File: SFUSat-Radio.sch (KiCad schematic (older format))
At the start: 1 part

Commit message: added jumpers for regulater EN and a jumper for fixing PA_ADJ. Connceted TRX_SIG to GPIO0
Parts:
- added JP? (x4): JUMPER, symbol JUMPER
- added R?: 457.8, symbol R
- added R?: 1k, symbol R
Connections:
- net labels added: EN_1V8, EN_3V3, EN_3V6, VCC_3.3, VCC_6.0_PW_IN
- wire segments 26 -> 38
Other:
- note added: "Jumper to fix ADJ to 2.25V or drive it externally.\nVoltage devider is 0.467=R_top * (G_bottom + 1/50k). \nSee SKY datasheet for 50k figure."
- note added: "Jumpers to fix regulators on or enable them externally"
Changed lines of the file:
@@
 F6 "SCLK" I L 3700 4600 60
 F7 "MISO" I L 3700 5100 60
-F8 "GPIO0" I L 3700 4300 60
-F9 "CSN" I L 3700 5350 60
-F10 "RX" I R 5200 4600 60
-F11 "TX" I R 5200 4900 60
-F12 "3V3" I R 5200 4125 60
-F13 "TRX_SIG" I R 5200 5250 60
-F14 "1V8" I R 5200 3875 60
+F8 "CSN" I L 3700 5350 60
+F9 "RX" I R 5200 4600 60
+F10 "TX" I R 5200 4900 60
+F11 "3V3" I R 5200 4125 60
+F12 "TRX_SIG" I R 5200 5250 60
+F13 "1V8" I R 5200 3875 60
 $EndSheet
 $Sheet
@@
 F6 "3V3" I R 8100 4600 60
 F7 "3V6" I R 8100 4800 60
-F8 "BYP" I L 6050 5650 60
+F8 "BYP" I L 6050 5550 60
 F9 "TRX_SIG" I L 6050 5250 60
+F10 "EN" I L 6050 5650 60
 $EndSheet
-Wire Wire Line
-	8100 5050 8700 5050
-Wire Wire Line
-	3250 4600 3700 4600
-Wire Wire Line
-	3700 4850 3350 4850
-Wire Wire Line
-	3450 5100 3700 5100
-Wire Wire Line
-	3500 5350 3700 5350
-Wire Wire Line
-	3700 5600 3600 5600
-Wire Wire Line
-	2800 3800 3700 3800
-Wire Wire Line
-	3700 4050 2950 4050
-Wire Wire Line
-	3100 4300 3700 4300
 $Comp
 L SMA J?
@@
 	1    0    0    -1
 $EndComp
-Wire Wire Line
-	8750 5250 8900 5250
-Connection ~ 8800 5250
-Connection ~ 8850 5250
-Wire Wire Line
-	5200 4600 6050 4600
-Wire Wire Line
-	6050 4900 5200 4900
 $Sheet
 S 5400 2550 1550 1100
@@
 F5 "1V8" I R 6950 3300 60
 $EndSheet
-Wire Wire Line
-	5400 3050 4650 3050
-Wire Wire Line
-	4650 3050 4650 3000
+$Comp
+L JUMPER JP?
+U 1 1 58778FEF
+P 4800 6700
+F 0 "JP?" H 4800 6850 50  0000 C CNN
+F 1 "JUMPER" H 4800 6620 50  0000 C CNN
+F 2 "" H 4800 6700 50  0000 C CNN
+F 3 "" H 4800 6700 50  0000 C CNN
+	1    4800 6700
+	1    0    0    -1
+$EndComp
+$Comp
+L R R?
+U 1 1 5877B3EF
+P 4300 6500
+F 0 "R?" V 4380 6500 50  0000 C CNN
+F 1 "457.8" V 4300 6500 50  0000 C CNN
+F 2 "" V 4230 6500 50  0000 C CNN
+F 3 "" H 4300 6500 50  0000 C CNN
+	1    4300 6500
+	1    0    0    -1
+$EndComp
+$Comp
+L R R?
+U 1 1 5877B4B0
+P 4300 6900
+F 0 "R?" V 4380 6900 50  0000 C CNN
+F 1 "1k" V 4300 6900 50  0000 C CNN
+F 2 "" V 4230 6900 50  0000 C CNN
+F 3 "" H 4300 6900 50  0000 C CNN
+	1    4300 6900
+	1    0    0    -1
+$EndComp
+$Comp
+L GND #PWR?
+U 1 1 5877B56F
+P 4300 7100
+F 0 "#PWR?" H 4300 6850 50  0001 C CNN
+F 1 "GND" H 4300 6950 50  0000 C CNN
+F 2 "" H 4300 7100 50  0000 C CNN
+F 3 "" H 4300 7100 50  0000 C CNN
+	1    4300 7100
+	1    0    0    -1
+$EndComp
+Text Label 4100 6350 0    60   ~ 0
+VCC_3.3
+Text Notes 3550 7650 0    60   ~ 0
+Jumper to fix ADJ to 2.25V or drive it externally.\nVoltage devider is 0.467=R_top * (G_bottom + 1/50k). \nSee SKY datasheet for 50k figure.
+Text Label 7100 3050 0    60   ~ 0
+VCC_3.3
+$Comp
+L JUMPER JP?
+U 1 1 587874C8
+P 5600 1150
+F 0 "JP?" H 5600 1300 50  0000 C CNN
+F 1 "JUMPER" H 5600 1070 50  0000 C CNN
+F 2 "" H 5600 1150 50  0000 C CNN
+F 3 "" H 5600 1150 50  0000 C CNN
+	1    5600 1150
+	1    0    0    -1
+$EndComp
+$Comp
+L JUMPER JP?
+U 1 1 5878759F
+P 5600 1550
+F 0 "JP?" H 5600 1700 50  0000 C CNN
+F 1 "JUMPER" H 5600 1470 50  0000 C CNN
+F 2 "" H 5600 1550 50  0000 C CNN
+F 3 "" H 5600 1550 50  0000 C CNN
+	1    5600 1550
+	1    0    0    -1
+$EndComp
+$Comp
+L JUMPER JP?
+U 1 1 58787662
+P 5600 1950
+F 0 "JP?" H 5600 2100 50  0000 C CNN
+F 1 "JUMPER" H 5600 1870 50  0000 C CNN
+F 2 "" H 5600 1950 50  0000 C CNN
+F 3 "" H 5600 1950 50  0000 C CNN
+	1    5600 1950
+	1    0    0    -1
+$EndComp
+Wire Wire Line
+	8100 5050 8700 5050
+Wire Wire Line
+	3250 4600 3700 4600
+Wire Wire Line
+	3700 4850 3350 4850
+Wire Wire Line
+	3450 5100 3700 5100
+Wire Wire Line
+	3500 5350 3700 5350
+Wire Wire Line
+	3700 5600 3600 5600
+Wire Wire Line
+	2800 3800 3700 3800
+Wire Wire Line
+	3700 4050 2950 4050
+Wire Wire Line
+	8750 5250 8900 5250
+Connection ~ 8800 5250
+Connection ~ 8850 5250
+Wire Wire Line
+	5200 4600 6050 4600
+Wire Wire Line
+	6050 4900 5200 4900
 Wire Wire Line
 	6950 3050 7400 3050
@@
 Wire Wire Line
 	7175 3300 6950 3300
+Wire Wire Line
+	4500 6700 4300 6700
+Wire Wire Line
+	4300 6650 4300 6750
+Connection ~ 4300 6700
+Wire Wire Line
+	4300 7050 4300 7100
+Wire Wire Line
+	4300 6350 4100 6350
+Wire Wire Line
+	6050 5450 5400 5450
+Wire Wire Line
+	5400 5450 5400 6700
+Wire Wire Line
+	5400 6700 5100 6700
+Wire Wire Line
+	5900 1150 6550 1150
+Wire Wire Line
+	5900 1550 6550 1550
+Wire Wire Line
+	5900 1950 6550 1950
+Wire Wire Line
+	5200 1950 5300 1950
+Wire Wire Line
+	4450 1550 5300 1550
+Wire Wire Line
+	5300 1150 5200 1150
+Wire Wire Line
+	5200 1150 5200 1950
+Connection ~ 5200 1550
+Text Label 4450 1550 0    60   ~ 0
+VCC_6.0_PW_IN
+Wire Wire Line
+	5400 3050 4450 3050
+Text Label 4450 3050 0    60   ~ 0
+VCC_6.0_PW_IN
+Text Label 6200 1150 0    60   ~ 0
+EN_3V6
+Text Label 6200 1550 0    60   ~ 0
+EN_3V3
+Text Label 6200 1950 0    60   ~ 0
+EN_1V8
+Text Notes 4550 900  0    60   ~ 0
+Jumpers to fix regulators on or enable them externally
 $EndSCHEMATC

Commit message: Added schematic of RT9183HGM5 (TO263-5)
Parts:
- removed JP? (x4): JUMPER, symbol JUMPER
- removed R?: 457.8, symbol R
- removed R?: 1k, symbol R
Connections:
- net labels removed: EN_1V8, EN_3V3, EN_3V6, VCC_3.3, VCC_6.0_PW_IN
- wire segments 38 -> 26
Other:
- note removed: "Jumper to fix ADJ to 2.25V or drive it externally.\nVoltage devider is 0.467=R_top * (G_bottom + 1/50k). \nSee SKY datasheet for 50k figure."
- note removed: "Jumpers to fix regulators on or enable them externally"
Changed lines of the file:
@@
 F6 "SCLK" I L 3700 4600 60
 F7 "MISO" I L 3700 5100 60
-F8 "CSN" I L 3700 5350 60
-F9 "RX" I R 5200 4600 60
-F10 "TX" I R 5200 4900 60
-F11 "3V3" I R 5200 4125 60
-F12 "TRX_SIG" I R 5200 5250 60
-F13 "1V8" I R 5200 3875 60
+F8 "GPIO0" I L 3700 4300 60
+F9 "CSN" I L 3700 5350 60
+F10 "RX" I R 5200 4600 60
+F11 "TX" I R 5200 4900 60
+F12 "3V3" I R 5200 4125 60
+F13 "TRX_SIG" I R 5200 5250 60
+F14 "1V8" I R 5200 3875 60
 $EndSheet
 $Sheet
@@
 F6 "3V3" I R 8100 4600 60
 F7 "3V6" I R 8100 4800 60
-F8 "BYP" I L 6050 5550 60
+F8 "BYP" I L 6050 5650 60
 F9 "TRX_SIG" I L 6050 5250 60
-F10 "EN" I L 6050 5650 60
 $EndSheet
+Wire Wire Line
+	8100 5050 8700 5050
+Wire Wire Line
+	3250 4600 3700 4600
+Wire Wire Line
+	3700 4850 3350 4850
+Wire Wire Line
+	3450 5100 3700 5100
+Wire Wire Line
+	3500 5350 3700 5350
+Wire Wire Line
+	3700 5600 3600 5600
+Wire Wire Line
+	2800 3800 3700 3800
+Wire Wire Line
+	3700 4050 2950 4050
+Wire Wire Line
+	3100 4300 3700 4300
 $Comp
 L SMA J?
@@
 	1    0    0    -1
 $EndComp
+Wire Wire Line
+	8750 5250 8900 5250
+Connection ~ 8800 5250
+Connection ~ 8850 5250
+Wire Wire Line
+	5200 4600 6050 4600
+Wire Wire Line
+	6050 4900 5200 4900
 $Sheet
 S 5400 2550 1550 1100
@@
 F5 "1V8" I R 6950 3300 60
 $EndSheet
-$Comp
-L JUMPER JP?
-U 1 1 58778FEF
-P 4800 6700
-F 0 "JP?" H 4800 6850 50  0000 C CNN
-F 1 "JUMPER" H 4800 6620 50  0000 C CNN
-F 2 "" H 4800 6700 50  0000 C CNN
-F 3 "" H 4800 6700 50  0000 C CNN
-	1    4800 6700
-	1    0    0    -1
-$EndComp
-$Comp
-L R R?
-U 1 1 5877B3EF
-P 4300 6500
-F 0 "R?" V 4380 6500 50  0000 C CNN
-F 1 "457.8" V 4300 6500 50  0000 C CNN
-F 2 "" V 4230 6500 50  0000 C CNN
-F 3 "" H 4300 6500 50  0000 C CNN
-	1    4300 6500
-	1    0    0    -1
-$EndComp
-$Comp
-L R R?
-U 1 1 5877B4B0
-P 4300 6900
-F 0 "R?" V 4380 6900 50  0000 C CNN
-F 1 "1k" V 4300 6900 50  0000 C CNN
-F 2 "" V 4230 6900 50  0000 C CNN
-F 3 "" H 4300 6900 50  0000 C CNN
-	1    4300 6900
-	1    0    0    -1
-$EndComp
-$Comp
-L GND #PWR?
-U 1 1 5877B56F
-P 4300 7100
-F 0 "#PWR?" H 4300 6850 50  0001 C CNN
-F 1 "GND" H 4300 6950 50  0000 C CNN
-F 2 "" H 4300 7100 50  0000 C CNN
-F 3 "" H 4300 7100 50  0000 C CNN
-	1    4300 7100
-	1    0    0    -1
-$EndComp
-Text Label 4100 6350 0    60   ~ 0
-VCC_3.3
-Text Notes 3550 7650 0    60   ~ 0
-Jumper to fix ADJ to 2.25V or drive it externally.\nVoltage devider is 0.467=R_top * (G_bottom + 1/50k). \nSee SKY datasheet for 50k figure.
-Text Label 7100 3050 0    60   ~ 0
-VCC_3.3
-$Comp
-L JUMPER JP?
-U 1 1 587874C8
-P 5600 1150
-F 0 "JP?" H 5600 1300 50  0000 C CNN
-F 1 "JUMPER" H 5600 1070 50  0000 C CNN
-F 2 "" H 5600 1150 50  0000 C CNN
-F 3 "" H 5600 1150 50  0000 C CNN
-	1    5600 1150
-	1    0    0    -1
-$EndComp
-$Comp
-L JUMPER JP?
-U 1 1 5878759F
-P 5600 1550
-F 0 "JP?" H 5600 1700 50  0000 C CNN
-F 1 "JUMPER" H 5600 1470 50  0000 C CNN
-F 2 "" H 5600 1550 50  0000 C CNN
-F 3 "" H 5600 1550 50  0000 C CNN
-	1    5600 1550
-	1    0    0    -1
-$EndComp
-$Comp
-L JUMPER JP?
-U 1 1 58787662
-P 5600 1950
-F 0 "JP?" H 5600 2100 50  0000 C CNN
-F 1 "JUMPER" H 5600 1870 50  0000 C CNN
-F 2 "" H 5600 1950 50  0000 C CNN
-F 3 "" H 5600 1950 50  0000 C CNN
-	1    5600 1950
-	1    0    0    -1
-$EndComp
 Wire Wire Line
-	8100 5050 8700 5050
+	5400 3050 4650 3050
 Wire Wire Line
-	3250 4600 3700 4600
-Wire Wire Line
-	3700 4850 3350 4850
-Wire Wire Line
-	3450 5100 3700 5100
-Wire Wire Line
-	3500 5350 3700 5350
-Wire Wire Line
-	3700 5600 3600 5600
-Wire Wire Line
-	2800 3800 3700 3800
-Wire Wire Line
-	3700 4050 2950 4050
-Wire Wire Line
-	8750 5250 8900 5250
-Connection ~ 8800 5250
-Connection ~ 8850 5250
-Wire Wire Line
-	5200 4600 6050 4600
-Wire Wire Line
-	6050 4900 5200 4900
+	4650 3050 4650 3000
 Wire Wire Line
 	6950 3050 7400 3050
@@
 Wire Wire Line
 	7175 3300 6950 3300
-Wire Wire Line
-	4500 6700 4300 6700
-Wire Wire Line
-	4300 6650 4300 6750
-Connection ~ 4300 6700
-Wire Wire Line
-	4300 7050 4300 7100
-Wire Wire Line
-	4300 6350 4100 6350
-Wire Wire Line
-	6050 5450 5400 5450
-Wire Wire Line
-	5400 5450 5400 6700
-Wire Wire Line
-	5400 6700 5100 6700
-Wire Wire Line
-	5900 1150 6550 1150
-Wire Wire Line
-	5900 1550 6550 1550
-Wire Wire Line
-	5900 1950 6550 1950
-Wire Wire Line
-	5200 1950 5300 1950
-Wire Wire Line
-	4450 1550 5300 1550
-Wire Wire Line
-	5300 1150 5200 1150
-Wire Wire Line
-	5200 1150 5200 1950
-Connection ~ 5200 1550
-Text Label 4450 1550 0    60   ~ 0
-VCC_6.0_PW_IN
-Wire Wire Line
-	5400 3050 4450 3050
-Text Label 4450 3050 0    60   ~ 0
-VCC_6.0_PW_IN
-Text Label 6200 1150 0    60   ~ 0
-EN_3V6
-Text Label 6200 1550 0    60   ~ 0
-EN_3V3
-Text Label 6200 1950 0    60   ~ 0
-EN_1V8
-Text Notes 4550 900  0    60   ~ 0
-Jumpers to fix regulators on or enable them externally
 $EndSCHEMATC

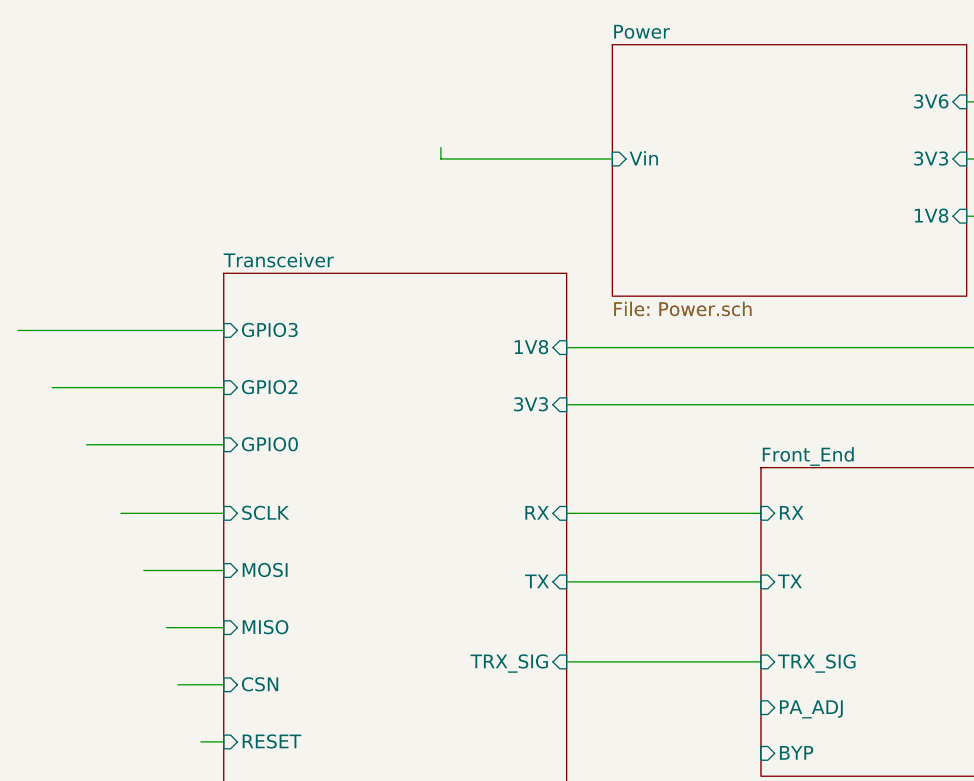
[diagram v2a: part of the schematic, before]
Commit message: moved jumpers into respective schematics
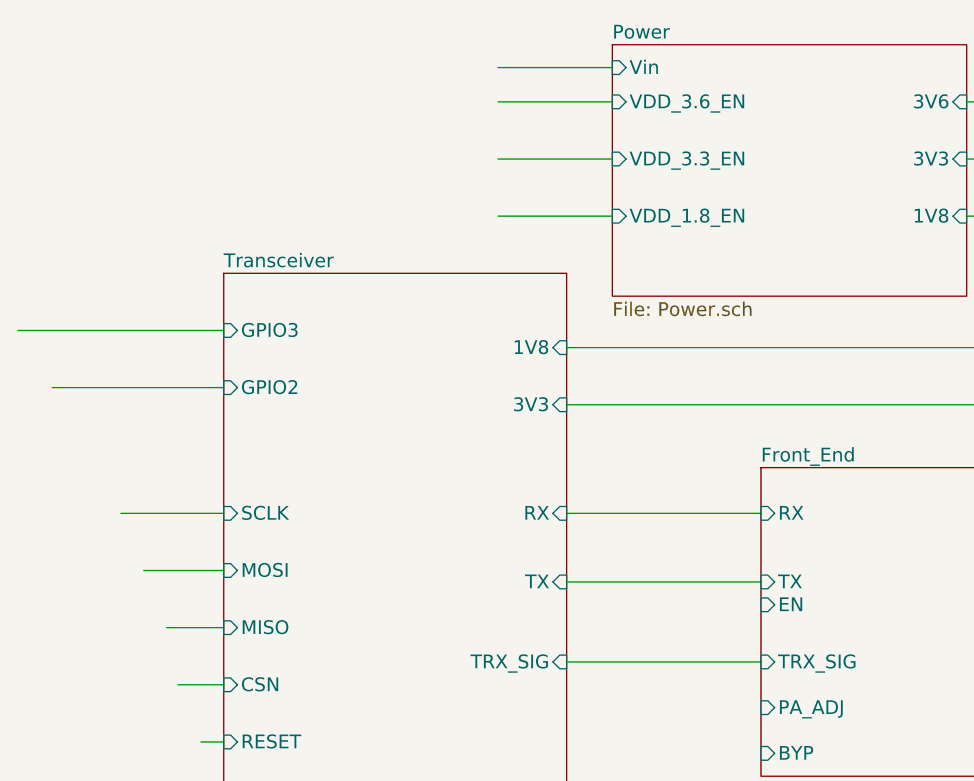
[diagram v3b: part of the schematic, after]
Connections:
- wire segments 26 -> 27
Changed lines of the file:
@@
 F6 "SCLK" I L 3700 4600 60
 F7 "MISO" I L 3700 5100 60
-F8 "GPIO0" I L 3700 4300 60
-F9 "CSN" I L 3700 5350 60
-F10 "RX" I R 5200 4600 60
-F11 "TX" I R 5200 4900 60
-F12 "3V3" I R 5200 4125 60
-F13 "TRX_SIG" I R 5200 5250 60
-F14 "1V8" I R 5200 3875 60
+F8 "CSN" I L 3700 5350 60
+F9 "RX" I R 5200 4600 60
+F10 "TX" I R 5200 4900 60
+F11 "3V3" I R 5200 4125 60
+F12 "TRX_SIG" I R 5200 5250 60
+F13 "1V8" I R 5200 3875 60
 $EndSheet
 $Sheet
@@
 F8 "BYP" I L 6050 5650 60
 F9 "TRX_SIG" I L 6050 5250 60
+F10 "EN" I L 6050 5000 60
 $EndSheet
 Wire Wire Line
@@
 Wire Wire Line
 	3700 4050 2950 4050
-Wire Wire Line
-	3100 4300 3700 4300
 $Comp
 L SMA J?
@@
 F0 "Power" 60
 F1 "Power.sch" 60
-F2 "Vin" I L 5400 3050 60
+F2 "Vin" I L 5400 2650 60
 F3 "3V3" I R 6950 3050 60
 F4 "3V6" I R 6950 2800 60
 F5 "1V8" I R 6950 3300 60
+F6 "VDD_1.8_EN" I L 5400 3300 60
+F7 "VDD_3.3_EN" I L 5400 3050 60
+F8 "VDD_3.6_EN" I L 5400 2800 60
 $EndSheet
-Wire Wire Line
-	5400 3050 4650 3050
-Wire Wire Line
-	4650 3050 4650 3000
 Wire Wire Line
 	6950 3050 7400 3050
@@
 Wire Wire Line
 	7175 3300 6950 3300
+Wire Wire Line
+	5400 2650 4900 2650
+Wire Wire Line
+	5400 2800 4900 2800
+Wire Wire Line
+	5400 3050 4900 3050
+Wire Wire Line
+	5400 3300 4900 3300
 $EndSCHEMATC
